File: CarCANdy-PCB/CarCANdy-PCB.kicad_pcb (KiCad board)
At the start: 2 copper layers, 2 parts, among them U1 Teensy4.1, U2 ESP32-C3_SUPERMINI_TH

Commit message: added to PCB
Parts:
- removed U1: Teensy4.1, Teensy:Teensy41
- added ADC1: RS, Jumper:SolderJumper-2_P1.3mm_Open_TrianglePad1.0x1.5mm, F.Cu at (36.3, 53.5)
- added C1: 100nF, Capacitor_SMD:C_0603_1608Metric_Pad1.08x0.95mm_HandSolder, F.Cu at (34.4, 57.5)
- added D1: NUP2105LT1G, nup2105lt1g:SOT95P237X111-3N, F.Cu at (127.5, 64.2)
- added D2: NUP2105LT1G, nup2105lt1g:SOT95P237X111-3N, F.Cu at (128.0, 74.9)
- added D3: NUP2105LT1G, nup2105lt1g:SOT95P237X111-3N, F.Cu at (128.7, 85.4)
- added D4: SS14, Diode_SMD:D_SMA, F.Cu at (75.5, 28.2)
- added D5: 1N4148W, Diode_SMD:D_SOD-123, F.Cu at (18.2, 20.5)
- added D6: BAT54S, Package_TO_SOT_SMD:SOT-23, F.Cu at (42.6, 56.3)
- added J1: 8P8C_Shielded, Connector_RJ:RJ45_RCH_RC01937, F.Cu at (151.3, 66.4)
- added J2: Power, Connector_JST:JST_EH_S3B-EH_1x03_P2.50mm_Horizontal, F.Cu at (149.1, 80.7)
- added JP2: RS, Connector_PinHeader_2.54mm:PinHeader_1x03_P2.54mm_Vertical, F.Cu at (127.5, 58.4)
- added JP6: RS, Connector_PinHeader_2.54mm:PinHeader_1x03_P2.54mm_Vertical, F.Cu at (127.9, 69.1)
- added JP9: RS, Connector_PinHeader_2.54mm:PinHeader_1x03_P2.54mm_Vertical, F.Cu at (128.7, 79.5)
- added K1: IM06TS, IM06:RELAY_IM06TS, F.Cu at (150.8, 95.1)
- added PSU1: 12v-5v_mini_buck, Library:mini12v-5v_buck, F.Cu at (135.6, 95.3)
- added R1: 120, Resistor_SMD:R_0603_1608Metric_Pad0.98x0.95mm_HandSolder, F.Cu at (133.9, 65.1)
- added R10: 33K, Resistor_SMD:R_0603_1608Metric_Pad0.98x0.95mm_HandSolder, F.Cu at (38.8, 62.4)
- added R11: 100, Resistor_SMD:R_0603_1608Metric_Pad0.98x0.95mm_HandSolder, F.Cu at (69.0, 35.8)
- added R12: 47k, Resistor_SMD:R_0603_1608Metric_Pad0.98x0.95mm_HandSolder, F.Cu at (68.9, 34.0)
- added R2: 10K, Resistor_SMD:R_0603_1608Metric_Pad0.98x0.95mm_HandSolder, F.Cu at (127.3, 61.2)
- added R3: 120, Resistor_SMD:R_0603_1608Metric_Pad0.98x0.95mm_HandSolder, F.Cu at (134.4, 75.9)
- added R4: 10K, Resistor_SMD:R_0603_1608Metric_Pad0.98x0.95mm_HandSolder, F.Cu at (127.8, 71.9)
- added R5: 120, Resistor_SMD:R_0603_1608Metric_Pad0.98x0.95mm_HandSolder, F.Cu at (135.1, 86.3)
- added R6: 10K, Resistor_SMD:R_0603_1608Metric_Pad0.98x0.95mm_HandSolder, F.Cu at (128.6, 82.4)
- added R7: 2.2K, Resistor_SMD:R_0603_1608Metric_Pad0.98x0.95mm_HandSolder, F.Cu at (17.0, 16.0)
- added R8: 10k, Resistor_SMD:R_0603_1608Metric_Pad0.98x0.95mm_HandSolder, F.Cu at (36.1, 18.5)
- added R9: 180K, Resistor_SMD:R_0603_1608Metric_Pad0.98x0.95mm_HandSolder, F.Cu at (38.8, 59.9)
- added RS1: RS, Jumper:SolderJumper-2_P1.3mm_Open_TrianglePad1.0x1.5mm, F.Cu at (130.9, 60.5)
- added RS2: RS, Jumper:SolderJumper-2_P1.3mm_Open_TrianglePad1.0x1.5mm, F.Cu at (131.4, 71.3)
- added RS3: RS, Jumper:SolderJumper-2_P1.3mm_Open_TrianglePad1.0x1.5mm, F.Cu at (132.1, 81.7)
- added T1: NTD5867NL, NTD5867NL:DPACK, F.Cu at (68.8, 26.5)
- added TERM1: TERM, Jumper:SolderJumper-2_P1.3mm_Open_TrianglePad1.0x1.5mm, F.Cu at (130.9, 64.2)
- added TERM2: TERM, Jumper:SolderJumper-2_P1.3mm_Open_TrianglePad1.0x1.5mm, F.Cu at (131.3, 75.0)
- added TERM3: TERM, Jumper:SolderJumper-2_P1.3mm_Open_TrianglePad1.0x1.5mm, F.Cu at (132.1, 85.4)
- added U3: SN65HVD233DR, SN65HVD233DR:SOIC127P599X175-8N, F.Cu at (121.6, 63.2)
- added U4: SN65HVD233DR, SN65HVD233DR:SOIC127P599X175-8N, F.Cu at (122.1, 73.9)
- added U5: SN65HVD233DR, SN65HVD233DR:SOIC127P599X175-8N, F.Cu at (122.9, 84.3)
- added U6: Teensy4.1, Teensy:Teensy41, F.Cu at (106.1, 85.0)
- added U7: LTV-817S, Package_DIP:SMDIP-4_W9.53mm, F.Cu at (26.0, 20.4)
- moved U2 29.0 mm to (63.1, 105.4), turned to -90 degrees
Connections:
- U2 pad 11: (no net) -> unconnected-(U2-GPIO10-Pad11)
- U2 pad 12: (no net) -> unconnected-(U2-GPIO11-Pad12)
- U2 pad 13: (no net) -> unconnected-(U2-GPIO12-Pad13)
- U2 pad 14: +3.3V -> unconnected-(U2-GPIO13-Pad14)

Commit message: added to PCB
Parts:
- removed ADC1: RS, Jumper:SolderJumper-2_P1.3mm_Open_TrianglePad1.0x1.5mm
- removed C1: 100nF, Capacitor_SMD:C_0603_1608Metric_Pad1.08x0.95mm_HandSolder
- removed D4: SS14, Diode_SMD:D_SMA
- removed D6: BAT54S, Package_TO_SOT_SMD:SOT-23
- removed K1: IM06TS, IM06:RELAY_IM06TS
- removed R10: 33K, Resistor_SMD:R_0603_1608Metric_Pad0.98x0.95mm_HandSolder
- removed R11: 100, Resistor_SMD:R_0603_1608Metric_Pad0.98x0.95mm_HandSolder
- removed R12: 47k, Resistor_SMD:R_0603_1608Metric_Pad0.98x0.95mm_HandSolder
- removed R9: 180K, Resistor_SMD:R_0603_1608Metric_Pad0.98x0.95mm_HandSolder
- removed T1: NTD5867NL, NTD5867NL:DPACK
- added C2: 100nF, Capacitor_SMD:C_0603_1608Metric_Pad1.08x0.95mm_HandSolder, F.Cu at (122.4, 86.4)
- added C3: 100nF, Capacitor_SMD:C_0603_1608Metric_Pad1.08x0.95mm_HandSolder, F.Cu at (89.2, 79.6)
- added C4: 100nF, Capacitor_SMD:C_0603_1608Metric_Pad1.08x0.95mm_HandSolder, F.Cu at (89.0, 88.6)
- added C5: 100nF, Capacitor_SMD:C_0603_1608Metric_Pad1.08x0.95mm_HandSolder, F.Cu at (89.2, 97.8)
- added C6: 100nF, Capacitor_SMD:C_0603_1608Metric_Pad1.08x0.95mm_HandSolder, F.Cu at (123.0, 92.1)
- added C7: 100nF, Capacitor_SMD:C_0603_1608Metric_Pad1.08x0.95mm_HandSolder, F.Cu at (150.0, 95.6)
- added D10: 1N4148W, Diode_SMD:D_SOD-123, F.Cu at (84.3, 72.6)
- added D11: 1N4148W, Diode_SMD:D_SOD-123, F.Cu at (86.8, 88.7)
- added D12: 1N4148W, Diode_SMD:D_SOD-123, F.Cu at (87.1, 97.8)
- added D13: BAT54S, Package_TO_SOT_SMD:SOT-23, F.Cu at (119.2, 93.7)
- added D14: BAT54S, Package_TO_SOT_SMD:SOT-23, F.Cu at (146.3, 97.2)
- added D7: BAT54S, Package_TO_SOT_SMD:SOT-23, F.Cu at (118.6, 88.2)
- added D8: 1N4148W, Diode_SMD:D_SOD-123, F.Cu at (87.0, 79.6)
- added D9: 1N4148W, Diode_SMD:D_SOD-123, F.Cu at (84.5, 65.2)
- added J3: TB004-508-03BE, TB004-508-03BE:CUI_TB004-508-03BE, F.Cu at (65.7, 55.7)
- added J4: AUART1, Connector_JST:JST_PH_S4B-PH-K_1x04_P2.00mm_Horizontal, F.Cu at (87.7, 109.1)
- added J5: TB004-508-03BE, TB004-508-03BE:CUI_TB004-508-03BE, F.Cu at (65.7, 87.9)
- added J6: TB004-508-03BE, TB004-508-03BE:CUI_TB004-508-03BE, F.Cu at (65.7, 103.9)
- added J7: TB004-508-03BE, TB004-508-03BE:CUI_TB004-508-03BE, F.Cu at (65.7, 72.0)
- added J8: AUART1, Connector_JST:JST_PH_S4B-PH-K_1x04_P2.00mm_Horizontal, F.Cu at (76.4, 109.1)
- added J9: TB004-508-03BE, TB004-508-03BE:CUI_TB004-508-03BE, F.Cu at (151.1, 104.7)
- added K3: IM02, IM06:RELAY_IM06TS, F.Cu at (80.3, 81.3)
- added K4: IM02, IM06:RELAY_IM06TS, F.Cu at (80.3, 90.3)
- added K5: IM02, IM06:RELAY_IM06TS, F.Cu at (80.3, 99.3)
- added Q1: AO3400A, Package_TO_SOT_SMD:SOT-23, F.Cu at (87.9, 84.0)
- added Q2: AO3400A, Package_TO_SOT_SMD:SOT-23, F.Cu at (87.9, 93.0)
- added Q3: AO3400A, Package_TO_SOT_SMD:SOT-23, F.Cu at (87.9, 101.9)
- added R13: 22K, Resistor_SMD:R_0603_1608Metric_Pad0.98x0.95mm_HandSolder, F.Cu at (122.4, 89.5)
- added R14: 33K, Resistor_SMD:R_0603_1608Metric_Pad0.98x0.95mm_HandSolder, F.Cu at (122.4, 88.0)
- added R15: 22K, Resistor_SMD:R_0603_1608Metric_Pad0.98x0.95mm_HandSolder, F.Cu at (123.0, 95.3)
- added R16: 33K, Resistor_SMD:R_0603_1608Metric_Pad0.98x0.95mm_HandSolder, F.Cu at (123.0, 93.7)
- added R17: 22K, Resistor_SMD:R_0603_1608Metric_Pad0.98x0.95mm_HandSolder, F.Cu at (150.0, 98.7)
- added R18: 33K, Resistor_SMD:R_0603_1608Metric_Pad0.98x0.95mm_HandSolder, F.Cu at (150.0, 97.1)
- added R19: 100, Resistor_SMD:R_0603_1608Metric_Pad0.98x0.95mm_HandSolder, F.Cu at (91.3, 79.5)
- added R20: 47K, Resistor_SMD:R_0603_1608Metric_Pad0.98x0.95mm_HandSolder, F.Cu at (91.1, 84.2)
- added R21: 2.2K, Resistor_SMD:R_0603_1608Metric_Pad0.98x0.95mm_HandSolder, F.Cu at (87.7, 62.2)
- added R22: 10k, Resistor_SMD:R_0603_1608Metric_Pad0.98x0.95mm_HandSolder, F.Cu at (93.2, 62.2)
- added R23: 2.2K, Resistor_SMD:R_0603_1608Metric_Pad0.98x0.95mm_HandSolder, F.Cu at (87.5, 69.6)
- added R24: 10k, Resistor_SMD:R_0603_1608Metric_Pad0.98x0.95mm_HandSolder, F.Cu at (92.9, 69.6)
- added R25: 100, Resistor_SMD:R_0603_1608Metric_Pad0.98x0.95mm_HandSolder, F.Cu at (91.3, 88.6)
- added R26: 47K, Resistor_SMD:R_0603_1608Metric_Pad0.98x0.95mm_HandSolder, F.Cu at (91.2, 92.9)
- added R27: 100, Resistor_SMD:R_0603_1608Metric_Pad0.98x0.95mm_HandSolder, F.Cu at (91.2, 97.8)
- added R28: 47K, Resistor_SMD:R_0603_1608Metric_Pad0.98x0.95mm_HandSolder, F.Cu at (91.2, 102.1)
- added SW2: JS202011CQN, JS202011CQN:JS202011CQN, F.Cu at (77.9, 58.0)
- added SW3: JS202011CQN, JS202011CQN:JS202011CQN, F.Cu at (78.0, 65.2)
- added SW4: JS202011CQN, JS202011CQN:JS202011CQN, F.Cu at (77.8, 72.6)
- added U1: LTV-357T, Package_SO:SO-4_4.4x3.6mm_P2.54mm, F.Cu at (90.4, 58.0)
- added U8: LTV-357T, Package_SO:SO-4_4.4x3.6mm_P2.54mm, F.Cu at (90.3, 72.7)
- J2: footprint Connector_JST:JST_EH_S3B-EH_1x03_P2.50mm_Horizontal -> Connector_JST:JST_EH_S2B-EH_1x02_P2.50mm_Horizontal
- U7: value LTV-817S -> LTV-357T; footprint Package_DIP:SMDIP-4_W9.53mm -> Package_SO:SO-4_4.4x3.6mm_P2.54mm
- moved R7 80.7 mm to (87.6, 55.0)
- moved U7 78.6 mm to (90.5, 65.3)
- moved D5 76.0 mm to (84.4, 58.0)
- moved R8 67.6 mm to (93.1, 55.0), turned to 180 degrees
- moved U2 64.7 mm to (127.8, 107.7)
- moved PSU1 14.6 mm to (147.3, 86.4)
- moved J1 7.77 mm to (143.6, 66.9), turned to 90 degrees
- moved J2 5.51 mm to (149.3, 75.2)
- moved R6 2.51 mm to (126.7, 80.7)
- moved D3 2.51 mm to (126.8, 83.7)
- moved JP9 2.51 mm to (126.8, 77.9)
- moved R5 2.51 mm to (133.3, 84.7)
- moved RS3 2.51 mm to (130.2, 80.0)
- moved TERM3 2.51 mm to (130.2, 83.7)
- moved U5 2.51 mm to (121.0, 82.7)
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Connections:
- D5 pad 2: GND -> Net-(D5-A)
- J2 pad 1: 12v_CONST -> +12V
- J2 pad 2: 12v_IGN -> GND
- R7 pad 1: 12V_INPUT -> Net-(SW2A-B)
- R8 pad 1: GPIO -> GPIO_IN1
- U6 pad 1: unconnected-(U6-GND-Pad1) -> GND
- U6 pad 14: unconnected-(U6-12_MISO_MQSL-Pad14) -> GPIO_OUT1
- U6 pad 16: unconnected-(U6-24_A10_TX6_SCL2-Pad16) -> ATX2
- U6 pad 17: unconnected-(U6-25_A11_RX6_SDA2-Pad17) -> ARX2
- U6 pad 18: unconnected-(U6-26_A12_MOSI1-Pad18) -> GPIO_OUT2
- U6 pad 19: unconnected-(U6-27_A13_SCK1-Pad19) -> GPIO_OUT3
- U6 pad 20: unconnected-(U6-28_RX7-Pad20) -> ARX1
- U6 pad 21: unconnected-(U6-29_TX7-Pad21) -> ATX1
- U6 pad 33: unconnected-(U6-41_A17-Pad33) -> ADC3
- U6 pad 34: unconnected-(U6-GND-Pad34) -> GND
- U6 pad 36: unconnected-(U6-14_A0_TX3_SPDIF_OUT-Pad36) -> ADC2
- U6 pad 37: unconnected-(U6-15_A1_RX3_SPDIF_IN-Pad37) -> ADC1
- U6 pad 4: unconnected-(U6-2_OUT2-Pad4) -> GPIO_IN1
- U6 pad 47: unconnected-(U6-GND-Pad47) -> GND
- U6 pad 5: unconnected-(U6-3_LRCLK2-Pad5) -> GPIO_IN2
- U6 pad 52: unconnected-(U6-GND-Pad52) -> GND
- U6 pad 6: unconnected-(U6-4_BCLK2-Pad6) -> GPIO_IN3
- U7 pad 1: Net-(D5-K) -> Net-(D9-K)
- U7 pad 2: GND -> Net-(D9-A)
- U7 pad 4: GPIO -> GPIO_IN2
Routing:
- net +5V: track 0.00 -> 217.3 mm
- net +12V: track 0.00 -> 126.9 mm
- net +3.3V: track 0.00 -> 122.6 mm, vias 0 -> 4
- net ADC3: track 0.00 -> 71.4 mm
- net CAN3_TX: track 0.00 -> 47.9 mm
- net CAN3_RX: track 0.00 -> 44.4 mm, vias 0 -> 2
- net T_RX->E_TX: track 0.00 -> 44.0 mm
- net T_TX->E_RX: track 0.00 -> 40.4 mm
- net 5V_SIG1: track 0.00 -> 34.1 mm
- net CAN3_L: track 0.00 -> 33.6 mm
- net 5V_SIG2: track 0.00 -> 33.2 mm
- net CAN3_H: track 0.00 -> 29.1 mm
- net CAN2_RX: track 0.00 -> 28.5 mm
- net ATX2: track 0.00 -> 27.7 mm
- net CAN2_L: track 0.00 -> 25.9 mm
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- added copper zone on B.Cu, net GND
- added copper zone on F.Cu, net GND
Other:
- board outline added: 101.8 x 68.5 mm
- board text added: "<L H>"
- board text added: "IN1"
- board text added: "IN2"
- board text added: "IN3"
- board text added: "NO C NC"
- board text added: "OUT1"

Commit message: added to PCB
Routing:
- net GND: track 1.59 -> 7.09 mm, vias 13 -> 15
- net +3.3V: track 122.6 -> 125.7 mm
- net CAN1_TX: track 12.2 -> 9.78 mm, vias 0 -> 1
- net CAN1_H: track 23.6 -> 24.6 mm

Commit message: added to PCB
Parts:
- removed C7: 100nF, Capacitor_SMD:C_0603_1608Metric_Pad1.08x0.95mm_HandSolder
- removed D14: BAT54S, Package_TO_SOT_SMD:SOT-23
- removed J3, J9: TB004-508-03BE, TB004-508-03BE:CUI_TB004-508-03BE
- removed R17: 22K, Resistor_SMD:R_0603_1608Metric_Pad0.98x0.95mm_HandSolder
- removed R18: 33K, Resistor_SMD:R_0603_1608Metric_Pad0.98x0.95mm_HandSolder
- added J10: ADC1, Connector_JST:JST_XH_S3B-XH-A-1_1x03_P2.50mm_Horizontal, F.Cu at (131.0, 111.9)
- added J11: ADC1, Connector_JST:JST_XH_S3B-XH-A-1_1x03_P2.50mm_Horizontal, F.Cu at (119.6, 111.9)
- added J13: Conn_01x02_Pin, Connector_JST:JST_XH_S2B-XH-A-1_1x02_P2.50mm_Horizontal, F.Cu at (58.9, 53.2)
- added J14: Conn_01x02_Pin, Connector_JST:JST_XH_S2B-XH-A-1_1x02_P2.50mm_Horizontal, F.Cu at (58.9, 62.4)
- added J15: Conn_01x02_Pin, Connector_JST:JST_XH_S2B-XH-A-1_1x02_P2.50mm_Horizontal, F.Cu at (58.9, 71.4)
- added JP1: VSEL, Connector_PinHeader_2.00mm:PinHeader_1x03_P2.00mm_Vertical, F.Cu at (71.0, 57.6)
- added JP3: VSEL, Connector_PinHeader_2.00mm:PinHeader_1x03_P2.00mm_Vertical, F.Cu at (70.7, 64.8)
- added JP4: VSEL, Connector_PinHeader_2.00mm:PinHeader_1x03_P2.00mm_Vertical, F.Cu at (70.7, 72.5)
- D1, D2, D3: footprint nup2105lt1g:SOT95P237X111-3N -> Package_TO_SOT_SMD:SOT-23-3
- J2: footprint Connector_JST:JST_EH_S2B-EH_1x02_P2.50mm_Horizontal -> Connector_JST:JST_VH_S2P-VH_1x02_P3.96mm_Horizontal
- J4, J8: footprint Connector_JST:JST_PH_S4B-PH-K_1x04_P2.00mm_Horizontal -> Connector_JST:JST_XH_S4B-XH-A-1_1x04_P2.50mm_Horizontal
- J5, J6, J7: value TB004-508-03BE -> JSTVH3; footprint TB004-508-03BE:CUI_TB004-508-03BE -> Connector_JST:JST_VH_S3P-VH_1x03_P3.96mm_Horizontal
- U1, U7, U8: footprint Package_SO:SO-4_4.4x3.6mm_P2.54mm -> Package_SO:SOP-4_3.8x4.1mm_P2.54mm
- moved U2 24.6 mm to (152.2, 104.3), turned to 180 degrees
- moved C2 19.9 mm to (135.2, 101.5), turned to -90 degrees
- moved D7 17.7 mm to (133.5, 97.8), turned to 90 degrees
- moved R14 17.7 mm to (133.7, 101.5), turned to -90 degrees
- moved R13 15.5 mm to (132.1, 101.5), turned to 90 degrees
- moved C6 9.49 mm to (123.8, 101.6), turned to -90 degrees
- moved J7 8.02 mm to (65.6, 80.0)
- moved R16 7.92 mm to (122.2, 101.6), turned to -90 degrees
- moved R15 6.74 mm to (120.6, 101.6), turned to 90 degrees
- moved J1 5.87 mm to (149.2, 65.0)
- moved J5 5.77 mm to (65.8, 93.7)
- moved PSU1 5.40 mm to (152.7, 86.4)
- moved J8 5.04 mm to (72.2, 111.8)
- moved D13 5.02 mm to (122.2, 97.8), turned to 90 degrees
- moved J6 3.24 mm to (65.9, 107.2)
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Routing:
- net ADC3: track 71.6 -> 0.00 mm
- net T_TX->E_RX: track 40.4 -> 77.6 mm, vias 0 -> 1
- net T_RX->E_TX: track 44.0 -> 77.7 mm, vias 0 -> 1
- net +12V: track 126.9 -> 152.3 mm
- net 5V_SIG1: track 34.1 -> 10.00 mm
- net 5V_SIG2: track 33.2 -> 9.98 mm
- net ADC1: track 13.8 -> 32.1 mm
- net 5V_SIG3: track 18.1 -> 0.00 mm
- net +5V: track 217.3 -> 235.1 mm
- net Net-(J13-Pin_2): track 0.00 -> 13.5 mm
- net Net-(J15-Pin_2): track 0.00 -> 13.3 mm
- net Net-(J14-Pin_2): track 0.00 -> 13.0 mm
- net 12V_SELECT_INPUT1: track 17.8 -> 25.6 mm
- net CAN1_L: track 21.1 -> 28.4 mm
- net CAN1_H: track 24.6 -> 31.4 mm
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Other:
- board size 101.8 x 68.5 mm -> 110 x 68 mm
- board text added: "GND<>12V"
- board text removed: "IN1"
- board text removed: "IN2"
- board text removed: "IN3"
- board text removed: "NO C NC"
- board text removed: "OUT1"

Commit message: added to PCB
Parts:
- JP2, JP6, JP9: footprint Connector_PinHeader_2.54mm:PinHeader_1x03_P2.54mm_Vertical -> Connector_PinHeader_2.00mm:PinHeader_1x03_P2.00mm_Vertical
- moved J6 138.5 mm to (-44.0, 22.9)
- moved J5 138.0 mm to (-44.0, 9.93)
- moved J7 137.4 mm to (-44.0, -2.97)
- moved J15 136.7 mm to (-49.8, -11.6)
- moved J14 136.4 mm to (-49.8, -20.1)
- moved JP9 136.1 mm to (18.7, -4.80)
- moved JP2 136.1 mm to (18.7, -26.0)
- moved JP6 136.1 mm to (18.7, -15.2)
- moved J13 136.0 mm to (-49.8, -28.6)
- moved PSU1 135.8 mm to (45.1, 3.49)
- moved R13 135.8 mm to (24.6, 18.6)
- moved C3 135.8 mm to (-18.4, -3.39)
- moved C4 135.8 mm to (-18.5, 5.71)
- moved D1 135.8 mm to (19.3, -20.4)
- moved D11 135.8 mm to (-20.7, 5.73)
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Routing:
- net +12V: track 152.3 -> 147.2 mm
- net Net-(J5-Pad1): track 17.6 -> 21.9 mm
- net Net-(J5-Pad2): track 16.2 -> 19.1 mm
- net Net-(J6-Pad1): track 19.4 -> 22.3 mm
- net Net-(J7-Pad1): track 16.8 -> 19.6 mm
- net ARX2: track 32.1 -> 34.2 mm
- net Net-(J7-Pad2): track 15.2 -> 17.3 mm
- net Net-(J7-Pad3): track 12.6 -> 14.6 mm
- net 12V_SELECT_INPUT1: track 25.6 -> 27.4 mm
- net Net-(J5-Pad3): track 14.3 -> 16.2 mm
- net 12V_SELECT_INPUT2: track 24.9 -> 26.4 mm
- net CAN1_H: track 31.4 -> 33.0 mm
- net CAN2_H: track 29.5 -> 31.0 mm
- net CAN2_L: track 30.1 -> 31.3 mm
- net 12V_SELECT_INPUT3: track 25.6 -> 26.7 mm
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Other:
- outline, holes or cut-outs redrawn

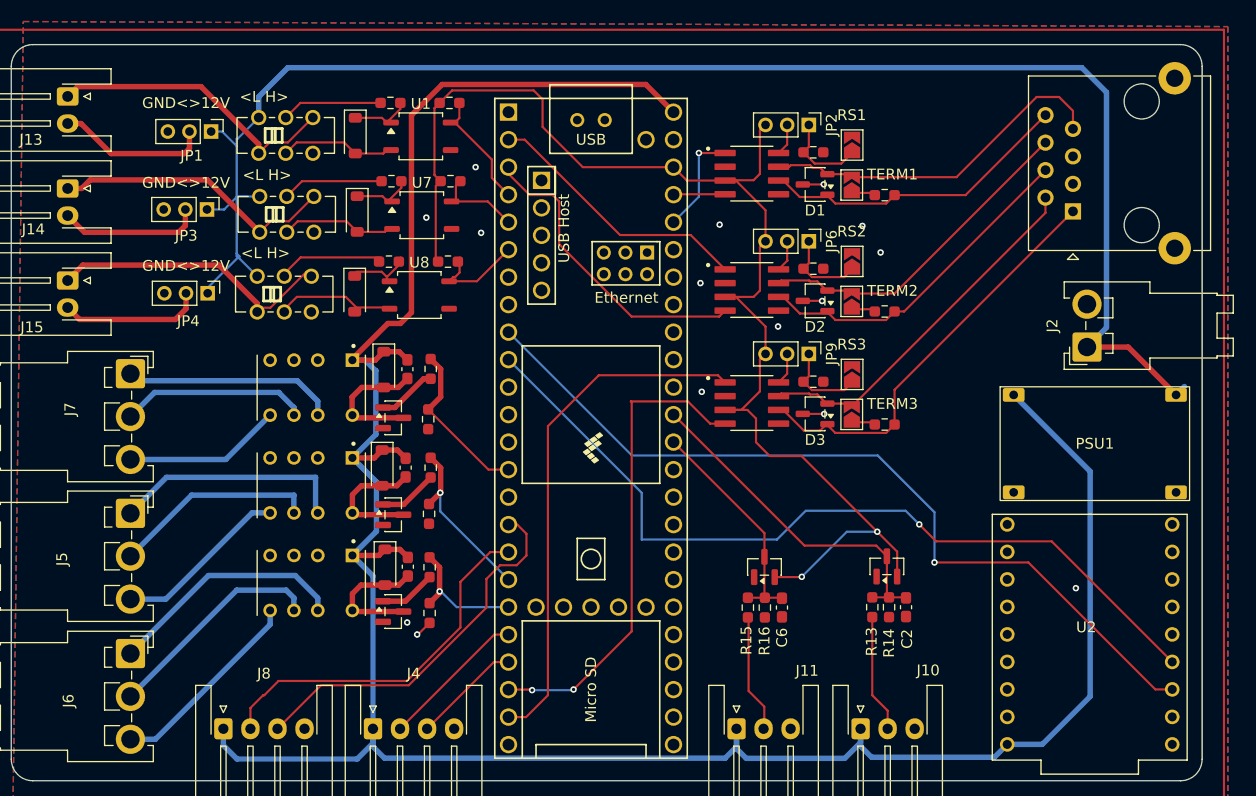
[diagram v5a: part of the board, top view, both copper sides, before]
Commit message: added aux ports header to teensy
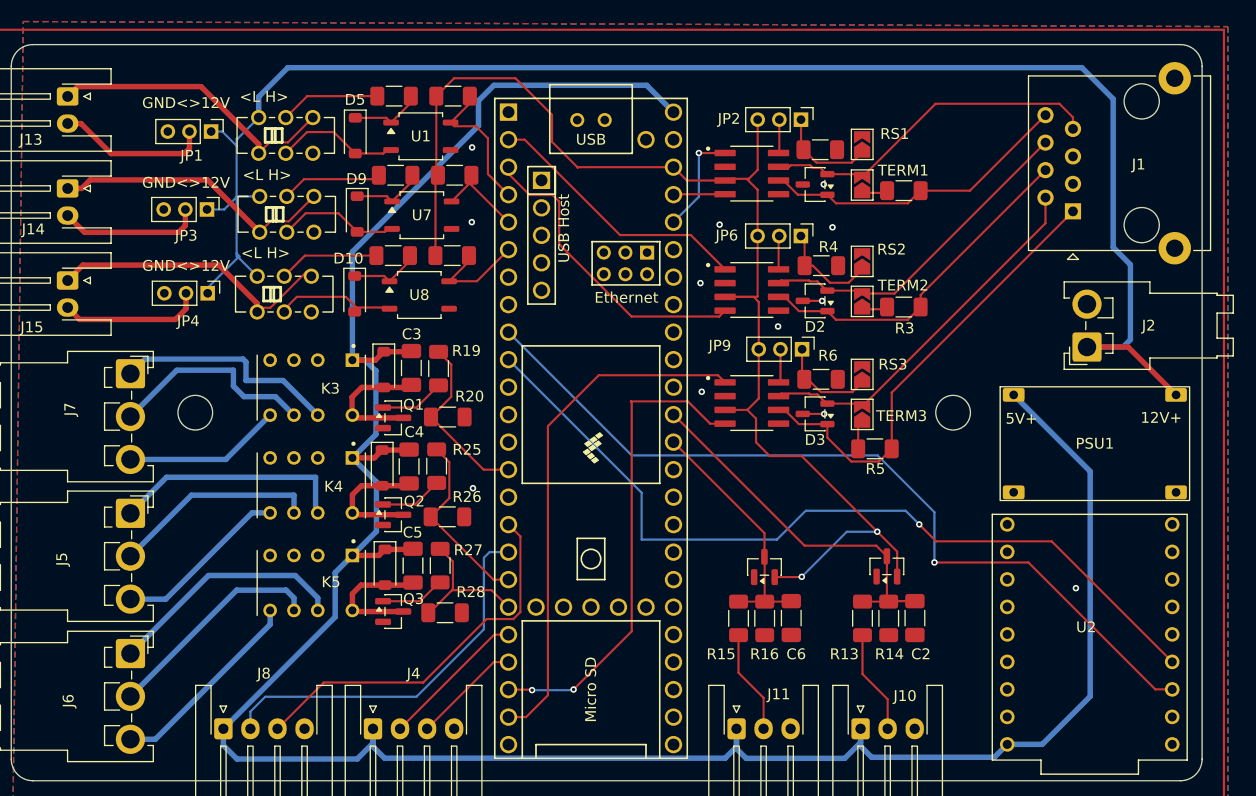
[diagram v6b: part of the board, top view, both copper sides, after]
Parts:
- added H1: MountingHole, MountingHole:MountingHole_3.2mm_M3, F.Cu at (-38.0, 0.63)
- added H2: MountingHole, MountingHole:MountingHole_3.2mm_M3, F.Cu at (32.0, 0.63)
- C2, C3, C4, C5, C6: footprint Capacitor_SMD:C_0603_1608Metric_Pad1.08x0.95mm_HandSolder -> Capacitor_SMD:C_1206_3216Metric_Pad1.33x1.80mm_HandSolder
- R1, R13, R14, R15, R16, R19, R2, R20, R21, R22, R23, R24, R25, R26, R27, R28, R3, R4, R5, R6, R7, R8: footprint Resistor_SMD:R_0603_1608Metric_Pad0.98x0.95mm_HandSolder -> Resistor_SMD:R_1206_3216Metric_Pad1.30x1.75mm_HandSolder
- moved R5 2.42 mm to (24.8, 3.97)
- moved R20 1.82 mm to (-14.7, 1.03), turned to 0 degrees
- moved R3 1.82 mm to (27.5, -9.13)
- moved R1 1.82 mm to (27.5, -19.9)
- moved R26 1.72 mm to (-14.7, 10.2), turned to 0 degrees
- moved R28 1.43 mm to (-14.9, 19.1), turned to 0 degrees
- moved R13 1.37 mm to (23.6, 19.6)
- moved R15 1.32 mm to (12.2, 19.6)
- moved C6 1.29 mm to (17.1, 19.6)
- moved C2 1.29 mm to (28.5, 19.6)
- moved R14 1.03 mm to (26.1, 19.6)
- moved R16 1.00 mm to (14.6, 19.6)
- moved R27 0.99 mm to (-15.4, 14.8)
- moved TERM1 0.96 mm to (23.6, -20.4)
- moved TERM2 0.96 mm to (23.6, -9.65)
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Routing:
- net CAN3_L: track 38.9 -> 42.5 mm
- net GND: track 7.09 -> 3.62 mm, vias 15 -> 12
- net GPIO_IN1: track 10.7 -> 13.2 mm
- net +12V: track 147.2 -> 149.4 mm
- net Net-(J7-Pad2): track 17.3 -> 19.4 mm
- net ADC1: track 32.1 -> 34.2 mm
- net ADC2: track 21.0 -> 23.1 mm
- net +3.3V: track 120.5 -> 118.8 mm
- net Net-(JP6-A): track 7.84 -> 9.37 mm
- net Net-(J7-Pad1): track 19.6 -> 21.0 mm
- net 5V_SIG2: track 10.9 -> 9.61 mm
- net GPIO_OUT3: track 12.0 -> 13.3 mm, vias 1 -> 0
- net GPIO_OUT2: track 15.7 -> 17.0 mm, vias 1 -> 0
- net 5V_SIG1: track 10.9 -> 9.61 mm
- net Net-(D5-K): track 5.43 -> 6.69 mm
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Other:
- board text added: "12V+"
- board text added: "5V+"
